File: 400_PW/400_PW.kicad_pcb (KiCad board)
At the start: 4 copper layers, 97.4 x 67.5 mm, 112 parts, among them J1 TESTBAT-14, J11 GND-7_21_22_3B_28_51B_53_76, J12 TESTBAT-14, J13 GND, J2 ON/OFF-6A, J3 +7.5V-13_26_33_51A_54_104_6A, J4 +4.9V-10_36_80_83_93, J5 -4.9V, J6 +48V, J7 ON/OFF-4A_6B, J8 15VIN-3A, J9 ON/OFF-48V, K1 BATT, U1 U_0064, U2 U_0064, U3 U_0064, U4 U_0126, U5 U_0089

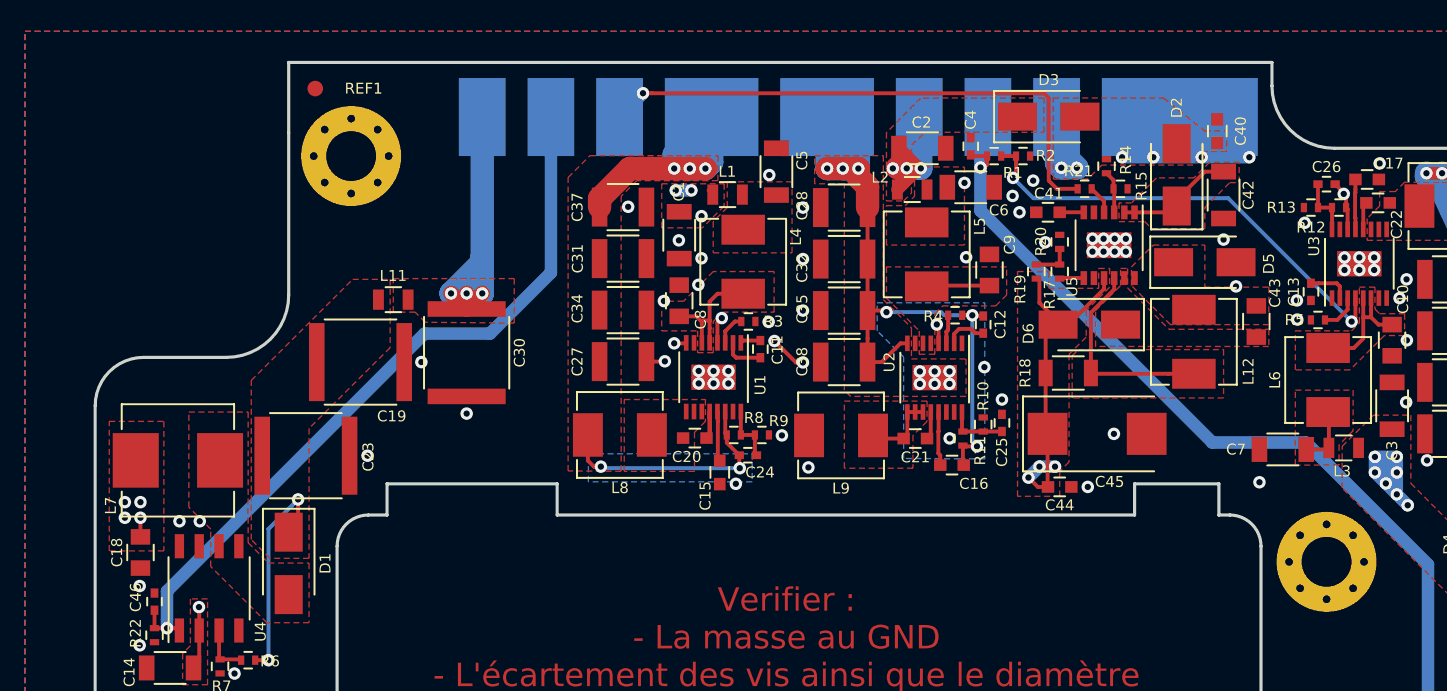
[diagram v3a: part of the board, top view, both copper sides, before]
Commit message: Add 1200_MIC schematic
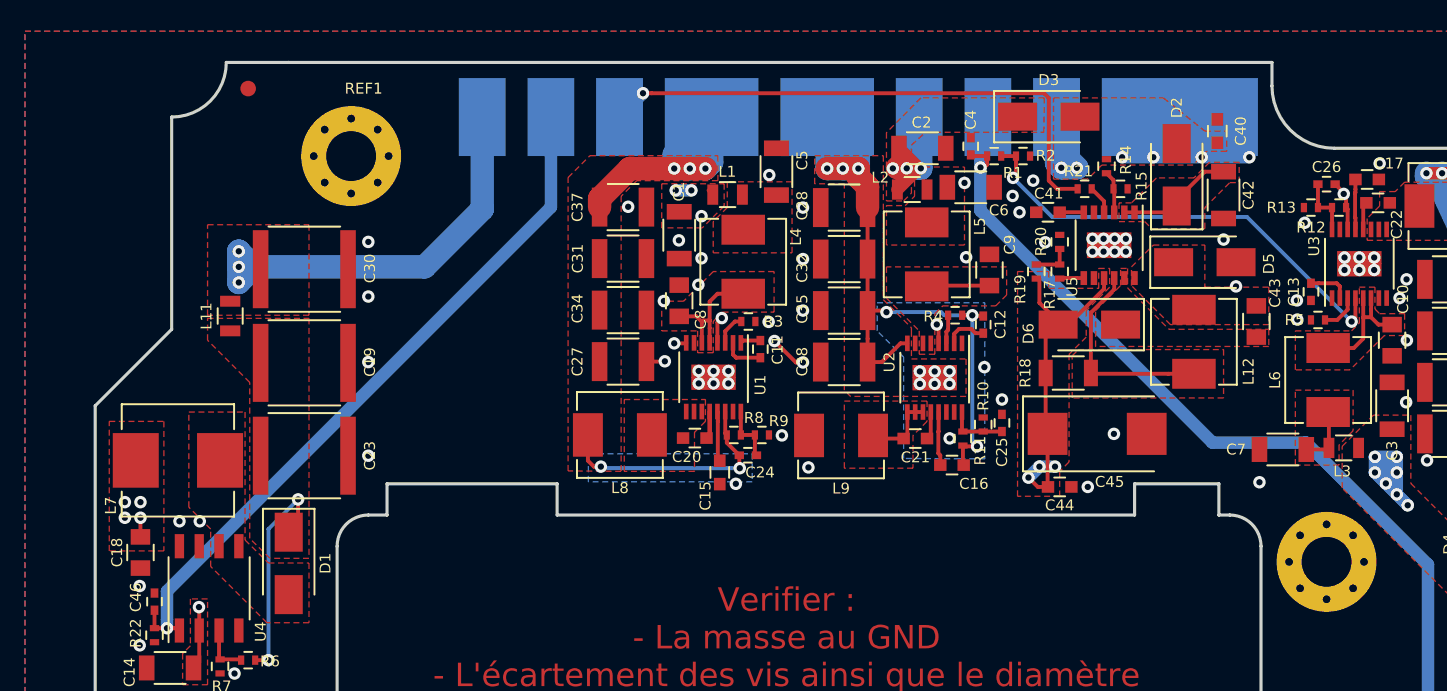
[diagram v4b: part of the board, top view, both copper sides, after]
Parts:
- moved C30 11.7 mm to (107.1, 87.1), turned to 180 degrees
- moved L11 10.5 mm to (102.3, 90.1), turned to 90 degrees
- moved REF1 4.30 mm to (103.5, 75.5)
- moved C19 3.60 mm to (107.1, 93.1)
- moved G*** 2.71 mm to (121.7, 95.2)
- moved C23 0.10 mm to (107.1, 99.0)
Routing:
- net GND: track 330.0 -> 325.5 mm, vias 75 -> 76
- net +48V: track 33.3 -> 28.9 mm
- net /EN_48V: track 48.9 -> 46.4 mm
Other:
- outline, holes or cut-outs redrawn

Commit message: First version preamp 1200
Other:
- board text added: "POWER -400- v1.0.0 PLF 2020"
- board text removed: "POWER -400- v1.0.0 PLF 2019"
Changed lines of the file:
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@@
-(kicad_pcb (version 20171130) (host pcbnew 5.1.4-e60b266~84~ubuntu18.04.1)
+(kicad_pcb (version 20171130) (host pcbnew 5.1.5-52549c5~84~ubuntu18.04.1)
   (general
     (thickness 1.6)
@@
   )
   (layers
-    (0 F.Cu signal)
-    (1 GND.Cu power)
-    (2 POWER.Cu power)
-    (31 B.Cu signal)
+    (0 F.Cu signal hide)
+    (1 GND.Cu power hide)
+    (2 POWER.Cu power hide)
+    (31 B.Cu signal hide)
     (32 B.Adhes user)
     (33 F.Adhes user)
@@
     (35 F.Paste user)
     (36 B.SilkS user hide)
-    (37 F.SilkS user)
+    (37 F.SilkS user hide)
     (38 B.Mask user)
     (39 F.Mask user hide)
@@
     (effects (font (size 1.5 1.5) (thickness 0.3)))
   )
-  (gr_text "POWER\n-400-\nv1.0.0\nPLF\n2019" (at 173.67 116.405) (layer B.Mask)
+  (gr_text "POWER\n-400-\nv1.0.0\nPLF\n2020" (at 173.67 116.405) (layer B.Mask)
     (effects (font (size 1 1) (thickness 0.15)) (justify mirror))
   )
